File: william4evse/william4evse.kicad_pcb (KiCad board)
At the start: 2 copper layers, 34 x 66 mm, 2 parts, among them J1 Boom_Precision_RJ45-B-1x1, U1 RCMB121

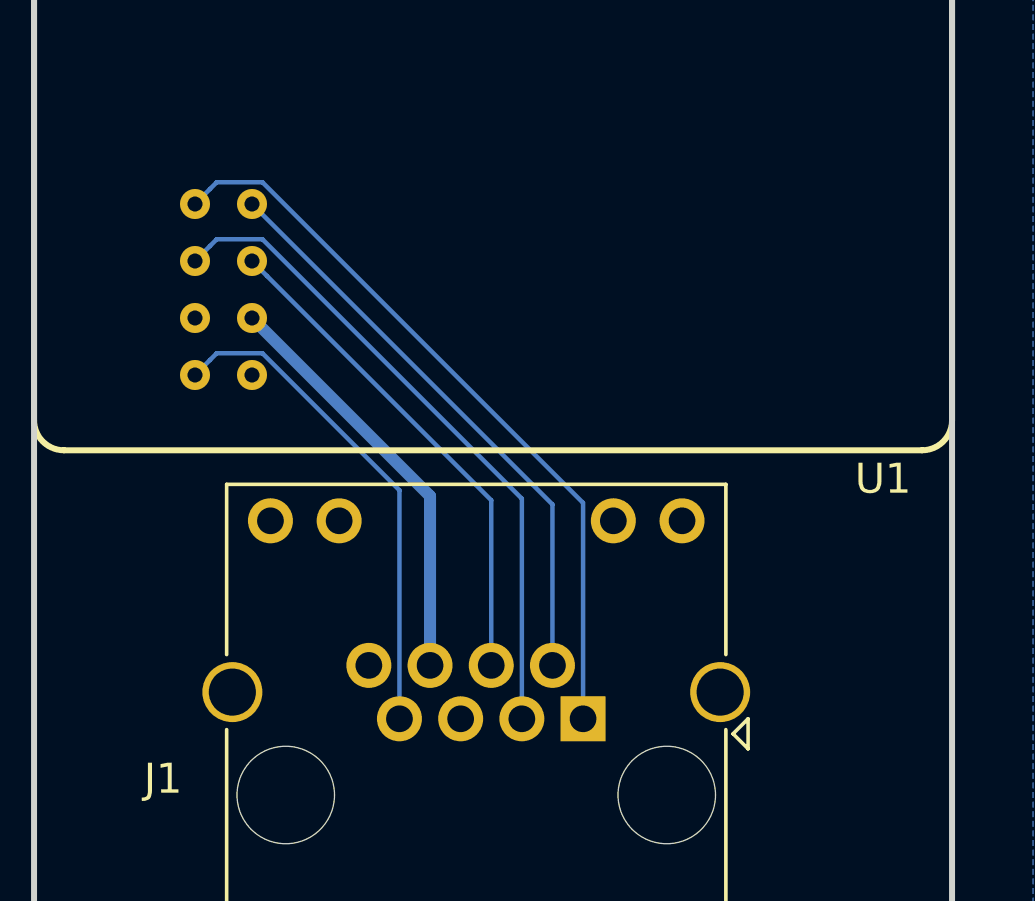
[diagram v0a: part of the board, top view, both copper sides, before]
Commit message: william/pcb: Update with fixed RCMB footprint
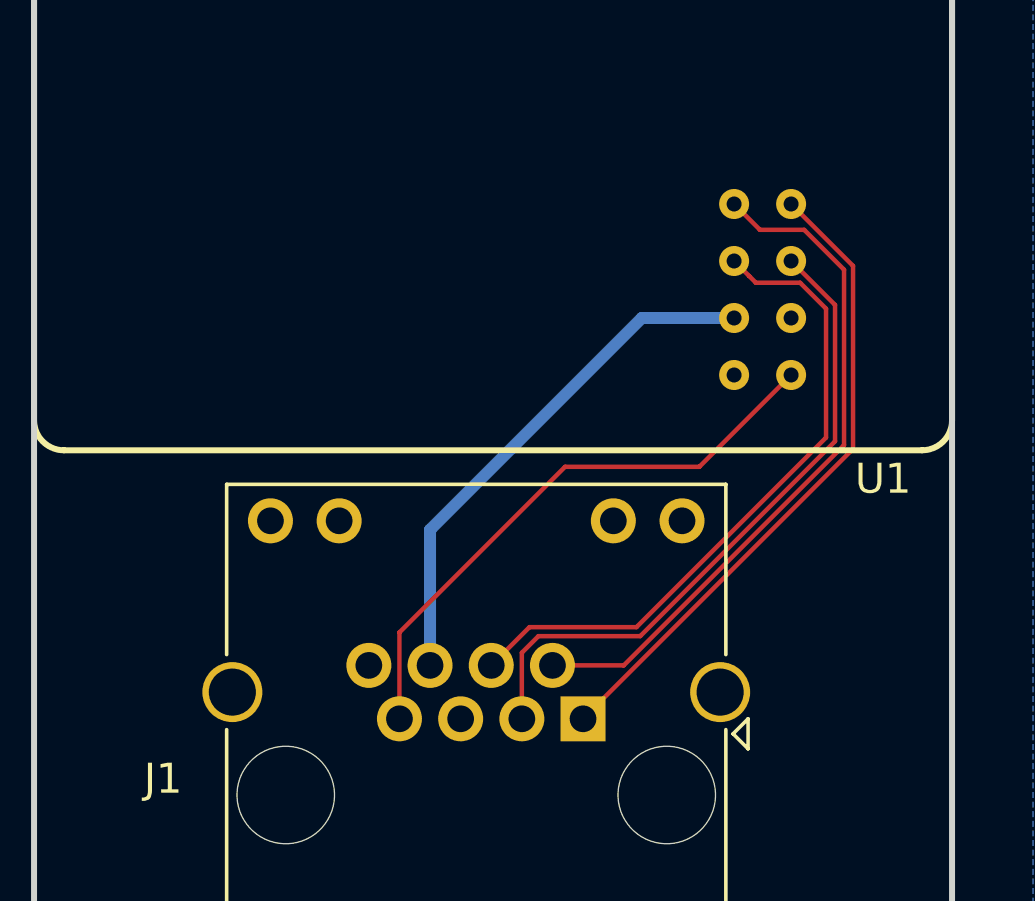
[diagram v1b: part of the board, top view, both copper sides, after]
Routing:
- net /X30_OUT: track 16.8 -> 22.3 mm
- net /TEST_IN: track 19.5 -> 23.2 mm
- net +5V: track 14.0 -> 17.6 mm
- net /ERROR_OUT: track 24.9 -> 21.7 mm
- net /PWM_OUT: track 16.6 -> 19.5 mm
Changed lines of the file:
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@@
-(kicad_pcb (version 20171130) (host pcbnew "(5.1.0)-1")
+(kicad_pcb (version 20171130) (host pcbnew 5.1.5)
   (general
     (thickness 1.6)
     (drawings 26)
-    (tracks 22)
+    (tracks 30)
     (zones 0)
     (modules 3)
@@
     (pad SH thru_hole circle (at 10.565 13.95) (size 2 2) (drill 0.8) (layers *.Cu *.Mask))
     (pad SH thru_hole circle (at -10.565 13.95) (size 2 2) (drill 0.8) (layers *.Cu *.Mask))
-    (pad 8 thru_hole circle (at -8.035 29.54) (size 1 1) (drill 0.5) (layers *.Cu *.Mask)
+    (pad 8 thru_hole circle (at 8.035 29.54) (size 1 1) (drill 0.5) (layers *.Cu *.Mask)
       (net 6 "Net-(U1-Pad8)"))
-    (pad 7 thru_hole circle (at -9.935 29.54) (size 1 1) (drill 0.5) (layers *.Cu *.Mask)
+    (pad 7 thru_hole circle (at 9.935 29.54) (size 1 1) (drill 0.5) (layers *.Cu *.Mask)
       (net 11 /PWM_OUT))
-    (pad 6 thru_hole circle (at -8.035 27.64) (size 1 1) (drill 0.5) (layers *.Cu *.Mask)
+    (pad 6 thru_hole circle (at 8.035 27.64) (size 1 1) (drill 0.5) (layers *.Cu *.Mask)
       (net 8 +5V))
-    (pad 5 thru_hole circle (at -9.935 27.64) (size 1 1) (drill 0.5) (layers *.Cu *.Mask)
+    (pad 5 thru_hole circle (at 9.935 27.64) (size 1 1) (drill 0.5) (layers *.Cu *.Mask)
       (net 7 GND))
-    (pad 4 thru_hole circle (at -8.035 25.74) (size 1 1) (drill 0.5) (layers *.Cu *.Mask)
+    (pad 4 thru_hole circle (at 8.035 25.74) (size 1 1) (drill 0.5) (layers *.Cu *.Mask)
       (net 9 /X30_OUT))
-    (pad 3 thru_hole circle (at -9.935 25.74) (size 1 1) (drill 0.5) (layers *.Cu *.Mask)
+    (pad 3 thru_hole circle (at 9.935 25.74) (size 1 1) (drill 0.5) (layers *.Cu *.Mask)
       (net 12 /X6_OUT))
-    (pad 2 thru_hole circle (at -8.035 23.84) (size 1 1) (drill 0.5) (layers *.Cu *.Mask)
+    (pad 2 thru_hole circle (at 8.035 23.84) (size 1 1) (drill 0.5) (layers *.Cu *.Mask)
       (net 10 /TEST_IN))
-    (pad 1 thru_hole circle (at -9.935 23.84) (size 1 1) (drill 0.5) (layers *.Cu *.Mask)
+    (pad 1 thru_hole circle (at 9.935 23.84) (size 1 1) (drill 0.5) (layers *.Cu *.Mask)
       (net 13 /ERROR_OUT))
     (model ${KIPRJMOD}/../ma4evse/3d/RCMB121.step
@@
     (arrow2b (pts (xy 164 60) (xy 164.586421 61.126504)))
   )
-  (gr_line (start 145 98) (end 145 104) (layer B.SilkS) (width 0.12))
-  (gr_text "ERROR_OUT\nX6_OUT\nGND\nPWM_OUT" (at 144 101) (layer B.SilkS)
+  (gr_line (start 138.4 98) (end 138.4 104) (layer B.SilkS) (width 0.12))
+  (gr_text "ERROR_OUT\nX6_OUT\nGND\nPWM_OUT" (at 139.4 101) (layer B.SilkS)
+    (effects (font (size 1 1) (thickness 0.15)) (justify right mirror))
+  )
+  (gr_text "TEST_IN\nX30_OUT\n+5V\nNC" (at 137.4 101) (layer B.SilkS)
     (effects (font (size 1 1) (thickness 0.15)) (justify left mirror))
-  )
-  (gr_text "TEST_IN\nX30_OUT\n+5V\nNC" (at 146 101) (layer B.SilkS)
-    (effects (font (size 1 1) (thickness 0.15)) (justify right mirror))
   )
   (gr_text "Dalton EVSE\n\"William\" board rev. 1.0\n(c) Tuetuopay 2019" (at 150 92) (layer B.SilkS)
@@
   (gr_arc (start 142 74) (end 153.71823 86.315968) (angle -92.84933975) (layer Edge.Cuts) (width 0.2))
   (gr_arc (start 142 74) (end 150.679595 59.382729) (angle -61.40287045) (layer Edge.Cuts) (width 0.2))
-  (segment (start 139.9 107.575) (end 133.965 101.64) (width 0.4) (layer B.Cu) (net 8))
-  (segment (start 139.9 113.22) (end 139.9 107.575) (width 0.4) (layer B.Cu) (net 8))
-  (segment (start 134.464999 100.239999) (end 133.965 99.74) (width 0.15) (layer B.Cu) (net 9))
-  (segment (start 141.94 113.22) (end 141.94 107.715) (width 0.15) (layer B.Cu) (net 9))
-  (segment (start 141.94 107.715) (end 134.464999 100.239999) (width 0.15) (layer B.Cu) (net 9))
-  (segment (start 143.98 107.855) (end 133.965 97.84) (width 0.15) (layer B.Cu) (net 10))
-  (segment (start 143.98 113.22) (end 143.98 107.855) (width 0.15) (layer B.Cu) (net 10))
-  (segment (start 132.564999 103.040001) (end 132.065 103.54) (width 0.15) (layer B.Cu) (net 11))
-  (segment (start 132.790001 102.814999) (end 132.564999 103.040001) (width 0.15) (layer B.Cu) (net 11))
-  (segment (start 134.313001 102.814999) (end 132.790001 102.814999) (width 0.15) (layer B.Cu) (net 11))
-  (segment (start 138.88 107.381998) (end 134.313001 102.814999) (width 0.15) (layer B.Cu) (net 11))
-  (segment (start 138.88 115) (end 138.88 107.381998) (width 0.15) (layer B.Cu) (net 11))
-  (segment (start 132.564999 99.240001) (end 132.065 99.74) (width 0.15) (layer B.Cu) (net 12))
-  (segment (start 132.790001 99.014999) (end 132.564999 99.240001) (width 0.15) (layer B.Cu) (net 12))
-  (segment (start 134.313001 99.014999) (end 132.790001 99.014999) (width 0.15) (layer B.Cu) (net 12))
-  (segment (start 142.96 107.661998) (end 134.313001 99.014999) (width 0.15) (layer B.Cu) (net 12))
-  (segment (start 142.96 115) (end 142.96 107.661998) (width 0.15) (layer B.Cu) (net 12))
-  (segment (start 132.564999 97.340001) (end 132.065 97.84) (width 0.15) (layer B.Cu) (net 13))
-  (segment (start 132.790001 97.114999) (end 132.564999 97.340001) (width 0.15) (layer B.Cu) (net 13))
-  (segment (start 134.313001 97.114999) (end 132.790001 97.114999) (width 0.15) (layer B.Cu) (net 13))
-  (segment (start 145 107.801998) (end 134.313001 97.114999) (width 0.15) (layer B.Cu) (net 13))
-  (segment (start 145 115) (end 145 107.801998) (width 0.15) (layer B.Cu) (net 13))
+  (segment (start 139.9 113.22) (end 139.9 108.7) (width 0.4) (layer B.Cu) (net 8))
+  (segment (start 146.96 101.64) (end 150.035 101.64) (width 0.4) (layer B.Cu) (net 8))
+  (segment (start 139.9 108.7) (end 146.96 101.64) (width 0.4) (layer B.Cu) (net 8))
+  (segment (start 150.760001 100.465001) (end 150.534999 100.239999) (width 0.15) (layer F.Cu) (net 9))
+  (segment (start 152.235723 100.465001) (end 150.760001 100.465001) (width 0.15) (layer F.Cu) (net 9))
+  (segment (start 141.94 113.22) (end 143.215011 111.944989) (width 0.15) (layer F.Cu) (net 9))
+  (segment (start 146.782177 111.944989) (end 153.09997 105.627196) (width 0.15) (layer F.Cu) (net 9))
+  (segment (start 150.534999 100.239999) (end 150.035 99.74) (width 0.15) (layer F.Cu) (net 9))
+  (segment (start 153.09997 105.627196) (end 153.09997 101.329248) (width 0.15) (layer F.Cu) (net 9))
+  (segment (start 143.215011 111.944989) (end 146.782177 111.944989) (width 0.15) (layer F.Cu) (net 9))
+  (segment (start 153.09997 101.329248) (end 152.235723 100.465001) (width 0.15) (layer F.Cu) (net 9))
+  (segment (start 143.98 113.22) (end 146.355722 113.22) (width 0.15) (layer F.Cu) (net 10))
+  (segment (start 146.355722 113.22) (end 153.69999 105.875732) (width 0.15) (layer F.Cu) (net 10))
+  (segment (start 153.69999 105.875732) (end 153.69999 100.029268) (width 0.15) (layer F.Cu) (net 10))
+  (segment (start 153.69999 100.029268) (end 152.370722 98.7) (width 0.15) (layer F.Cu) (net 10))
+  (segment (start 150.895 98.7) (end 150.035 97.84) (width 0.15) (layer F.Cu) (net 10))
+  (segment (start 152.370722 98.7) (end 150.895 98.7) (width 0.15) (layer F.Cu) (net 10))
+  (segment (start 138.88 115) (end 138.88 112.12) (width 0.15) (layer F.Cu) (net 11))
+  (segment (start 138.88 112.12) (end 144.4 106.6) (width 0.15) (layer F.Cu) (net 11))
+  (segment (start 148.875 106.6) (end 151.935 103.54) (width 0.15) (layer F.Cu) (net 11))
+  (segment (start 144.4 106.6) (end 148.875 106.6) (width 0.15) (layer F.Cu) (net 11))
+  (segment (start 143.511999 112.244999) (end 146.906445 112.244999) (width 0.15) (layer F.Cu) (net 12))
+  (segment (start 142.96 115) (end 142.96 112.796998) (width 0.15) (layer F.Cu) (net 12))
+  (segment (start 142.96 112.796998) (end 143.511999 112.244999) (width 0.15) (layer F.Cu) (net 12))
+  (segment (start 146.906445 112.244999) (end 153.39998 105.751464) (width 0.15) (layer F.Cu) (net 12))
+  (segment (start 153.39998 101.20498) (end 151.935 99.74) (width 0.15) (layer F.Cu) (net 12))
+  (segment (start 153.39998 105.751464) (end 153.39998 101.20498) (width 0.15) (layer F.Cu) (net 12))
+  (segment (start 145 115) (end 154 106) (width 0.15) (layer F.Cu) (net 13))
+  (segment (start 154 99.905) (end 151.935 97.84) (width 0.15) (layer F.Cu) (net 13))
+  (segment (start 154 106) (end 154 99.905) (width 0.15) (layer F.Cu) (net 13))
   (zone (net 7) (net_name GND) (layer F.Cu) (hatch edge 0.508)
     (connect_pads (clearance 0.15))

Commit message: william: Rev. 1.1
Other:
- board text added: "Dalton EVSE "William" board rev. 1.1 (c) Tuetuopay 2019 - 2020"
- board text removed: "Dalton EVSE "William" board rev. 1.0 (c) Tuetuopay 2019"
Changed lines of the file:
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@@
     (effects (font (size 1 1) (thickness 0.15)) (justify left mirror))
   )
-  (gr_text "Dalton EVSE\n\"William\" board rev. 1.0\n(c) Tuetuopay 2019" (at 150 92) (layer B.SilkS)
+  (gr_text "Dalton EVSE\n\"William\" board rev. 1.1\n(c) Tuetuopay 2019 - 2020" (at 150 92) (layer B.SilkS)
     (effects (font (size 1 1) (thickness 0.15)) (justify left mirror))
   )

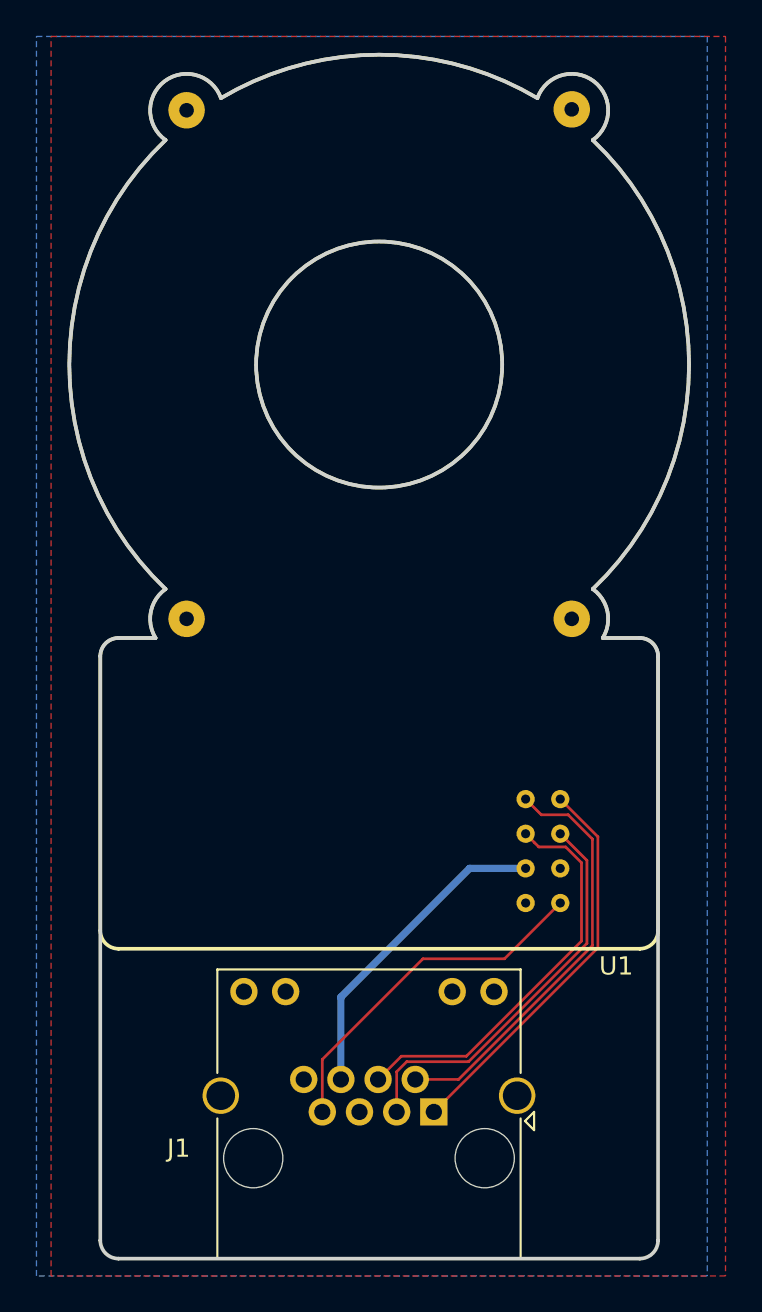
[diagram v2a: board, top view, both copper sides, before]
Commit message: william: Add err_out relay output
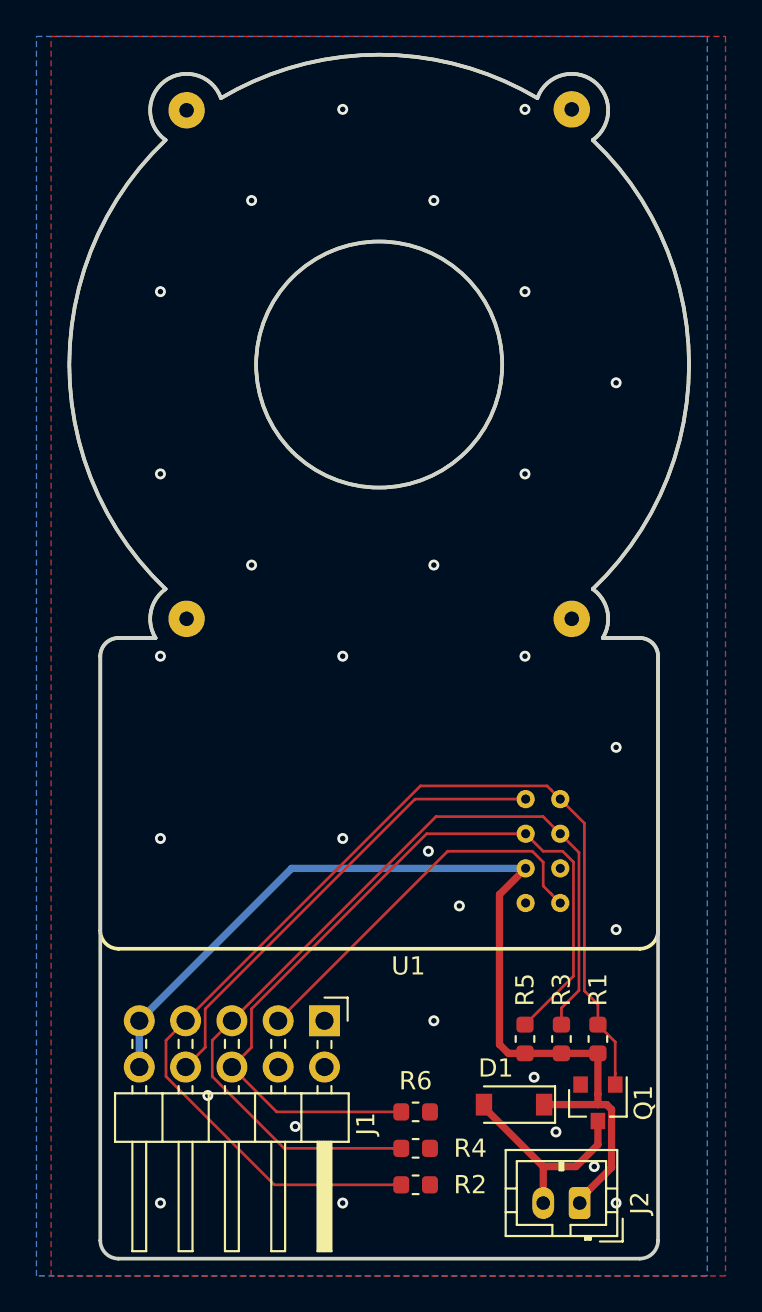
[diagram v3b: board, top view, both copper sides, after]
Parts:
- added D1: D_Schottky_Small, Diode_SMD:D_SOD-123, F.Cu at (149.4, 114.6)
- added J2: Conn_01x02, Connector_JST:JST_PH_B2B-PH-K_1x02_P2.00mm_Vertical, F.Cu at (153.0, 120.0)
- added Q1: AO3402, Package_TO_SOT_SMD:SOT-23, F.Cu at (154.0, 114.5)
- added R1: 10k, Resistor_SMD:R_0603_1608Metric, F.Cu at (154.0, 111.0)
- added R2: 20k, Resistor_SMD:R_0603_1608Metric, F.Cu at (144.0, 119.0)
- added R3: 10k, Resistor_SMD:R_0603_1608Metric, F.Cu at (152.0, 111.0)
- added R4: 20k, Resistor_SMD:R_0603_1608Metric, F.Cu at (144.0, 117.0)
- added R5: 10k, Resistor_SMD:R_0603_1608Metric, F.Cu at (150.0, 111.0)
- added R6: 20k, Resistor_SMD:R_0603_1608Metric, F.Cu at (144.0, 115.0)
- J1: value Boom_Precision_RJ45-B-1x1 -> Conn_02x05_Odd_Even; footprint Connector_RJ:RJ45_Amphenol_RJHSE538X -> Connector_PinHeader_2.54mm:PinHeader_2x05_P2.54mm_Horizontal
- moved J1 7.81 mm to (139.0, 110.0), turned to 270 degrees
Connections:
- J1 pad 1: /ERROR_OUT -> GND
- J1 pad 10: Net-(J1-Pad10) -> +5V
- J1 pad 2: /TEST_IN -> GND
- J1 pad 3: /X6_OUT -> /PWM_OUT
- J1 pad 4: /X30_OUT -> Net-(J1-Pad4)
- J1 pad 5: GND -> /X6_OUT
- J1 pad 6: +5V -> /X30_OUT
- J1 pad 7: /PWM_OUT -> /ERROR_OUT
- J1 pad 8: Net-(J1-Pad8) -> /TEST_IN
- J1 pad 9: Net-(J1-Pad9) -> +5V
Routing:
- net /ERROR_OUT: track 21.7 -> 62.0 mm
- net +5V: track 17.6 -> 55.5 mm
- net /X6_OUT: track 22.2 -> 49.8 mm
- net /X30_OUT: track 22.3 -> 46.3 mm
- net Net-(D1-Pad2): track 0.00 -> 11.5 mm
- net /TEST_IN: track 23.2 -> 26.0 mm
- net /PWM_OUT: track 19.5 -> 21.3 mm
- net GND: vias 0 -> 29
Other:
- net class Default: via_dia 0.8 -> 0.6; via_drill 0.4 -> 0.3
- net class Power: via_dia 0.8 -> 0.6; via_drill 0.4 -> 0.3
- rule via_min_size: 0.4 -> 0.6

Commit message: william: Revert "Add err_out relay output"
This reverts commit fe4c97044222ea82c6b882aa488b85d2dc32cb0e.
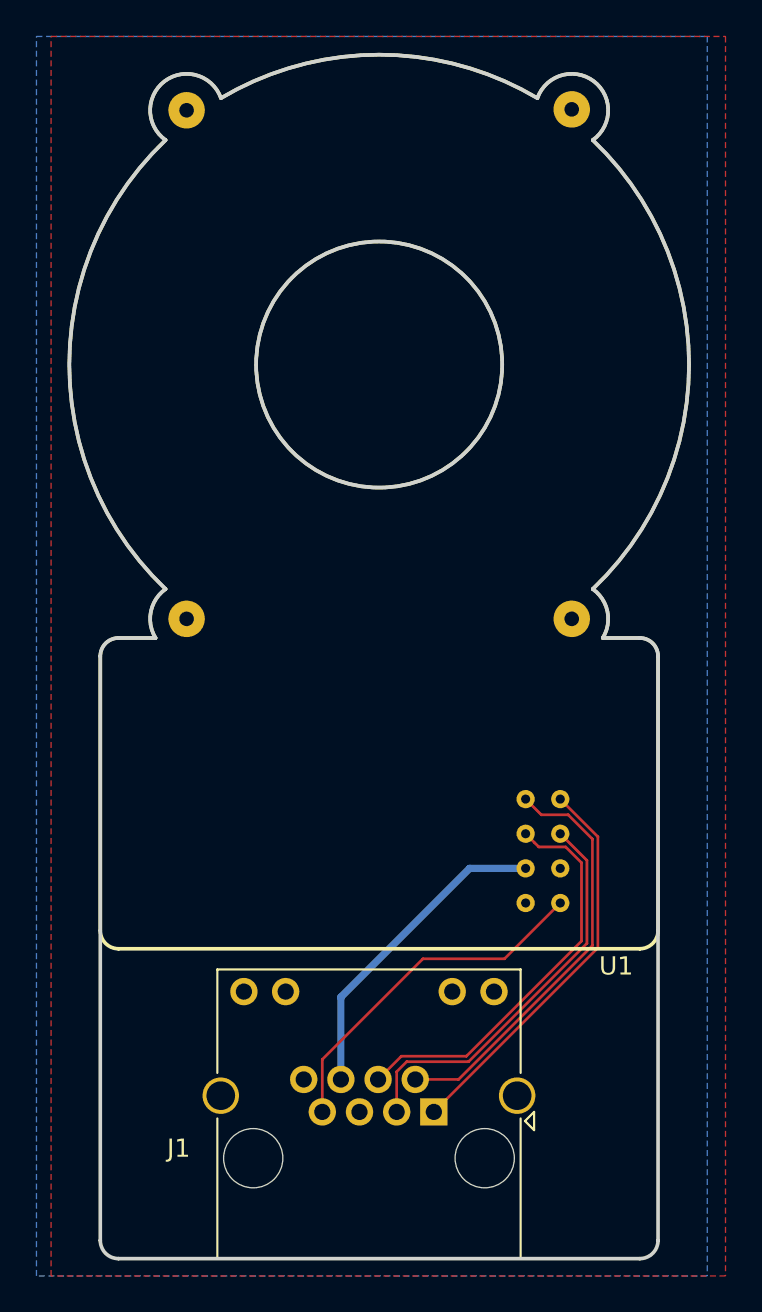
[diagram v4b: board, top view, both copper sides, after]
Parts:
- removed D1: D_Schottky_Small, Diode_SMD:D_SOD-123
- removed J2: Conn_01x02, Connector_JST:JST_PH_B2B-PH-K_1x02_P2.00mm_Vertical
- removed Q1: AO3402, Package_TO_SOT_SMD:SOT-23
- removed R1, R3, R5: 10k, Resistor_SMD:R_0603_1608Metric
- removed R2, R4, R6: 20k, Resistor_SMD:R_0603_1608Metric
- J1: value Conn_02x05_Odd_Even -> Boom_Precision_RJ45-B-1x1; footprint Connector_PinHeader_2.54mm:PinHeader_2x05_P2.54mm_Horizontal -> Connector_RJ:RJ45_Amphenol_RJHSE538X
- moved J1 7.81 mm to (145.0, 115.0), turned to 180 degrees
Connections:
- J1 pad 1: GND -> /ERROR_OUT
- J1 pad 10: +5V -> Net-(J1-Pad10)
- J1 pad 2: GND -> /TEST_IN
- J1 pad 3: /PWM_OUT -> /X6_OUT
- J1 pad 4: Net-(J1-Pad4) -> /X30_OUT
- J1 pad 5: /X6_OUT -> GND
- J1 pad 6: /X30_OUT -> +5V
- J1 pad 7: /ERROR_OUT -> /PWM_OUT
- J1 pad 8: /TEST_IN -> Net-(J1-Pad8)
- J1 pad 9: +5V -> Net-(J1-Pad9)
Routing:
- net /ERROR_OUT: track 62.0 -> 21.7 mm
- net +5V: track 55.5 -> 17.6 mm
- net /X6_OUT: track 49.8 -> 22.2 mm
- net /X30_OUT: track 46.3 -> 22.3 mm
- net Net-(D1-Pad2): track 11.5 -> 0.00 mm
- net /TEST_IN: track 26.0 -> 23.2 mm
- net /PWM_OUT: track 21.3 -> 19.5 mm
- net GND: vias 29 -> 0
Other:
- net class Default: via_dia 0.6 -> 0.8; via_drill 0.3 -> 0.4
- net class Power: via_dia 0.6 -> 0.8; via_drill 0.3 -> 0.4
- rule via_min_size: 0.6 -> 0.4
